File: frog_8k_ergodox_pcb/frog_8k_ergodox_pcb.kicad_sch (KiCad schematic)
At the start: 3 parts, among them J1 USB_C_Receptacle_USB2.0_14P, U1 PMW3360DM-T2QU, U2 STM32F072CBTx

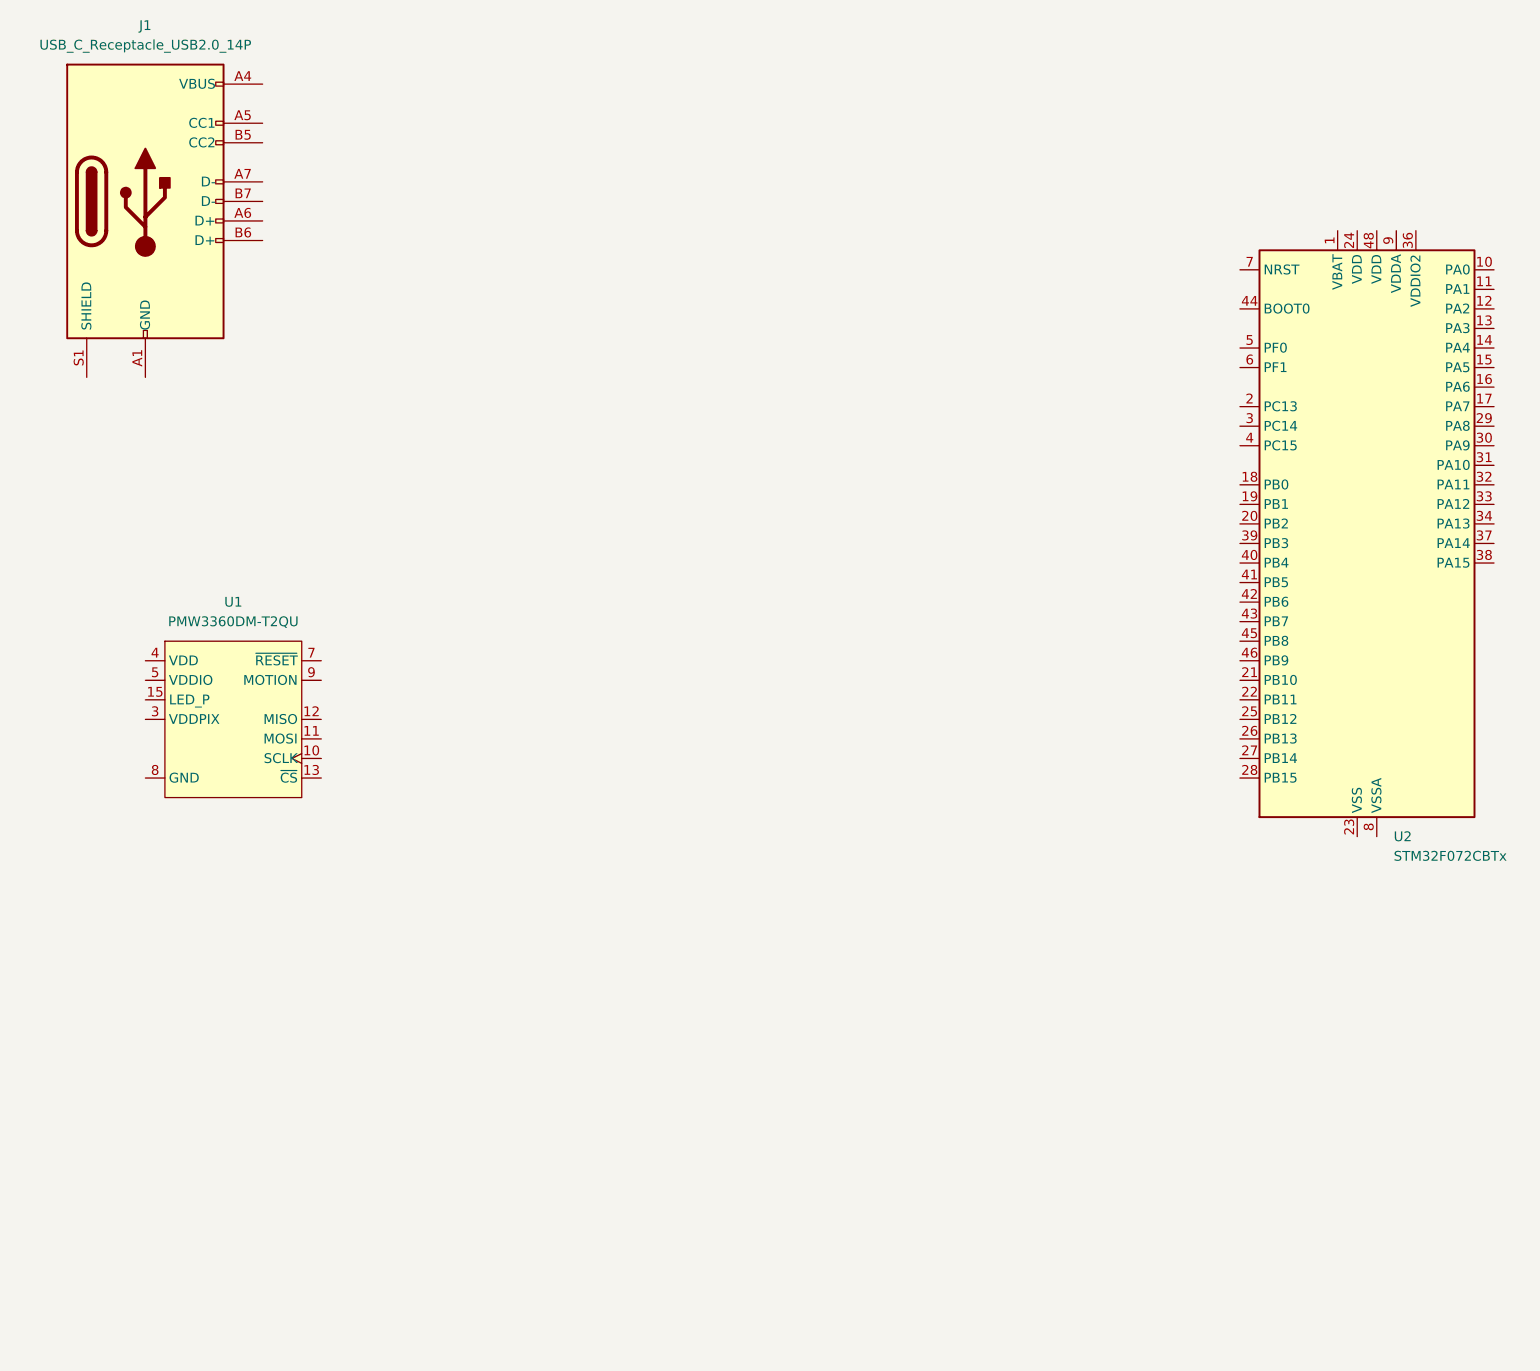
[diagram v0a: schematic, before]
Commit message: Added 3v3 power and gnd symbol
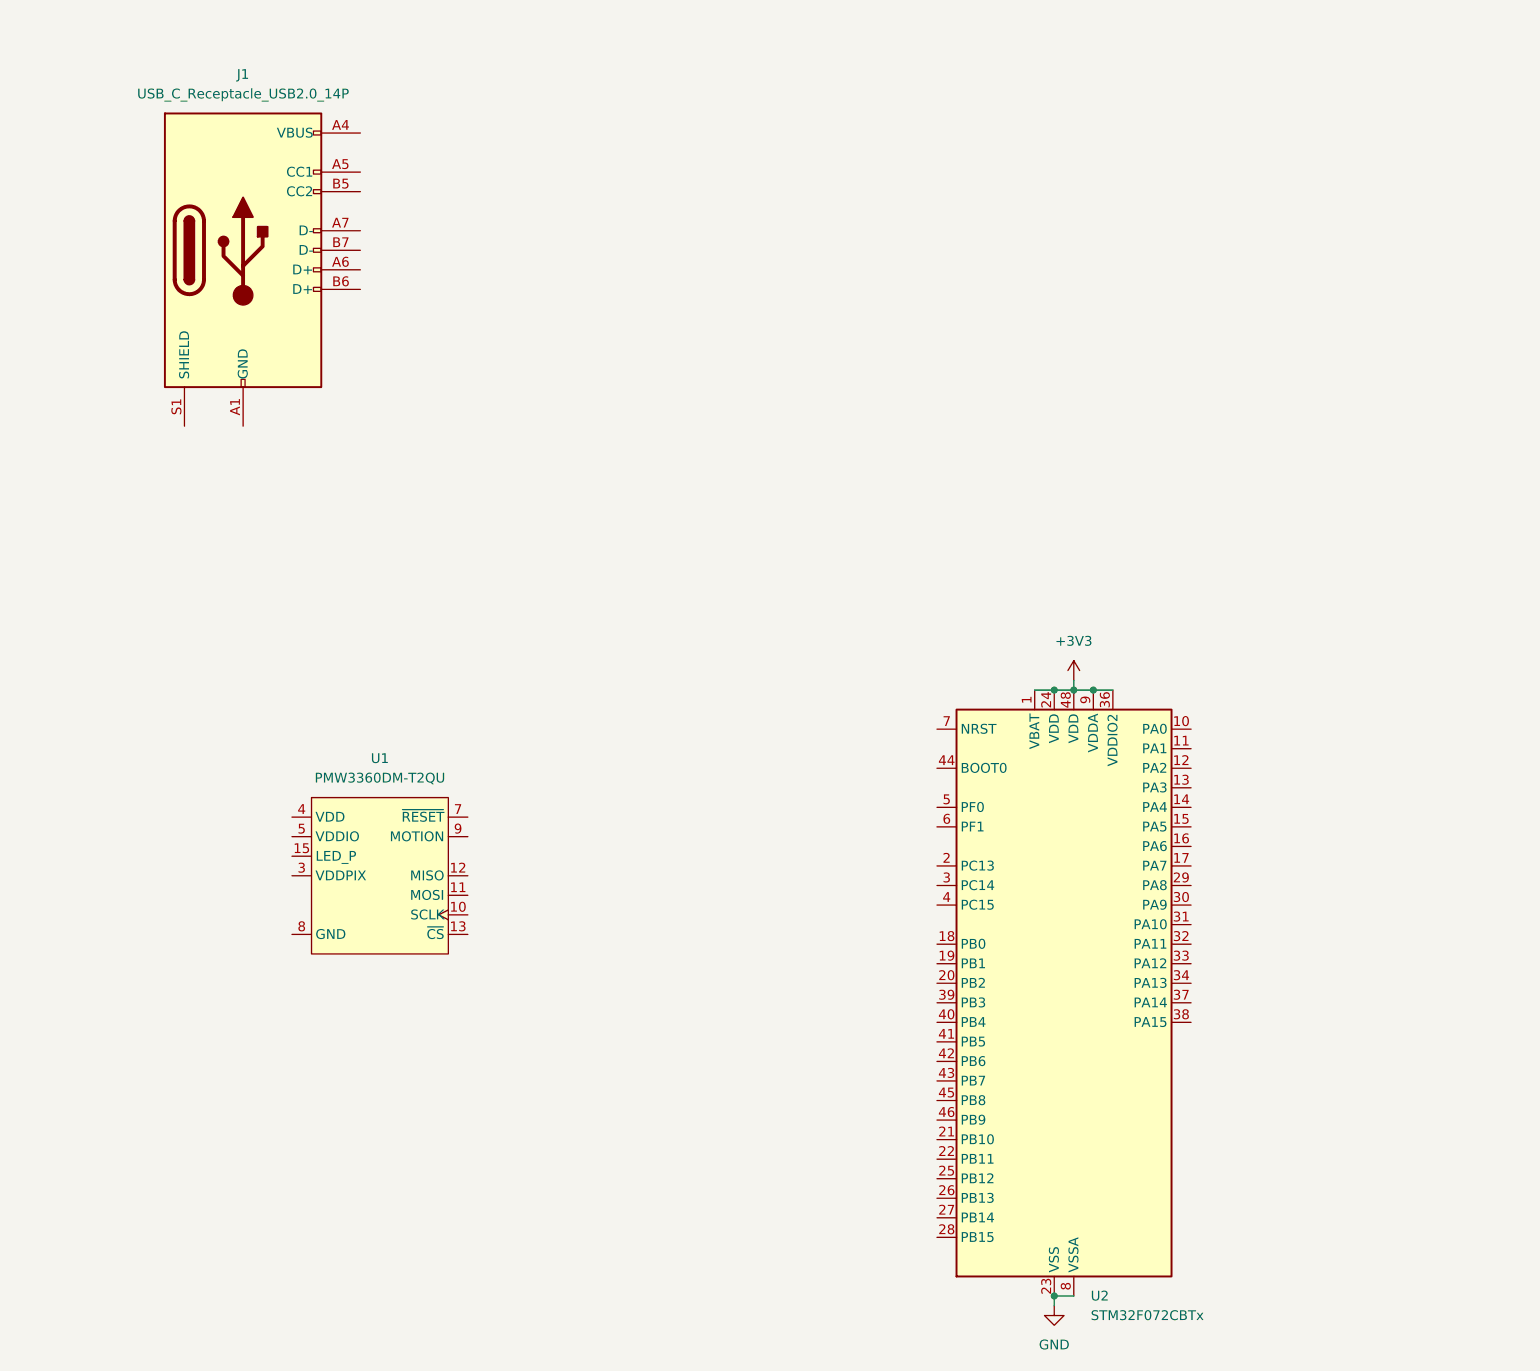
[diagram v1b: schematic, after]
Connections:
- net +3V3: now reaches U2.1 (VBAT)
- net +3V3: now also U2.24 (VDD), U2.36 (VDDIO2), U2.48 (VDD), U2.9 (VDDA)
- net GND: now reaches U2.23 (VSS), U2.35 (VSS), U2.47 (VSS)
- net GND: now also U2.8 (VSSA)
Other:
- moved on the sheet: J1, U1, U2

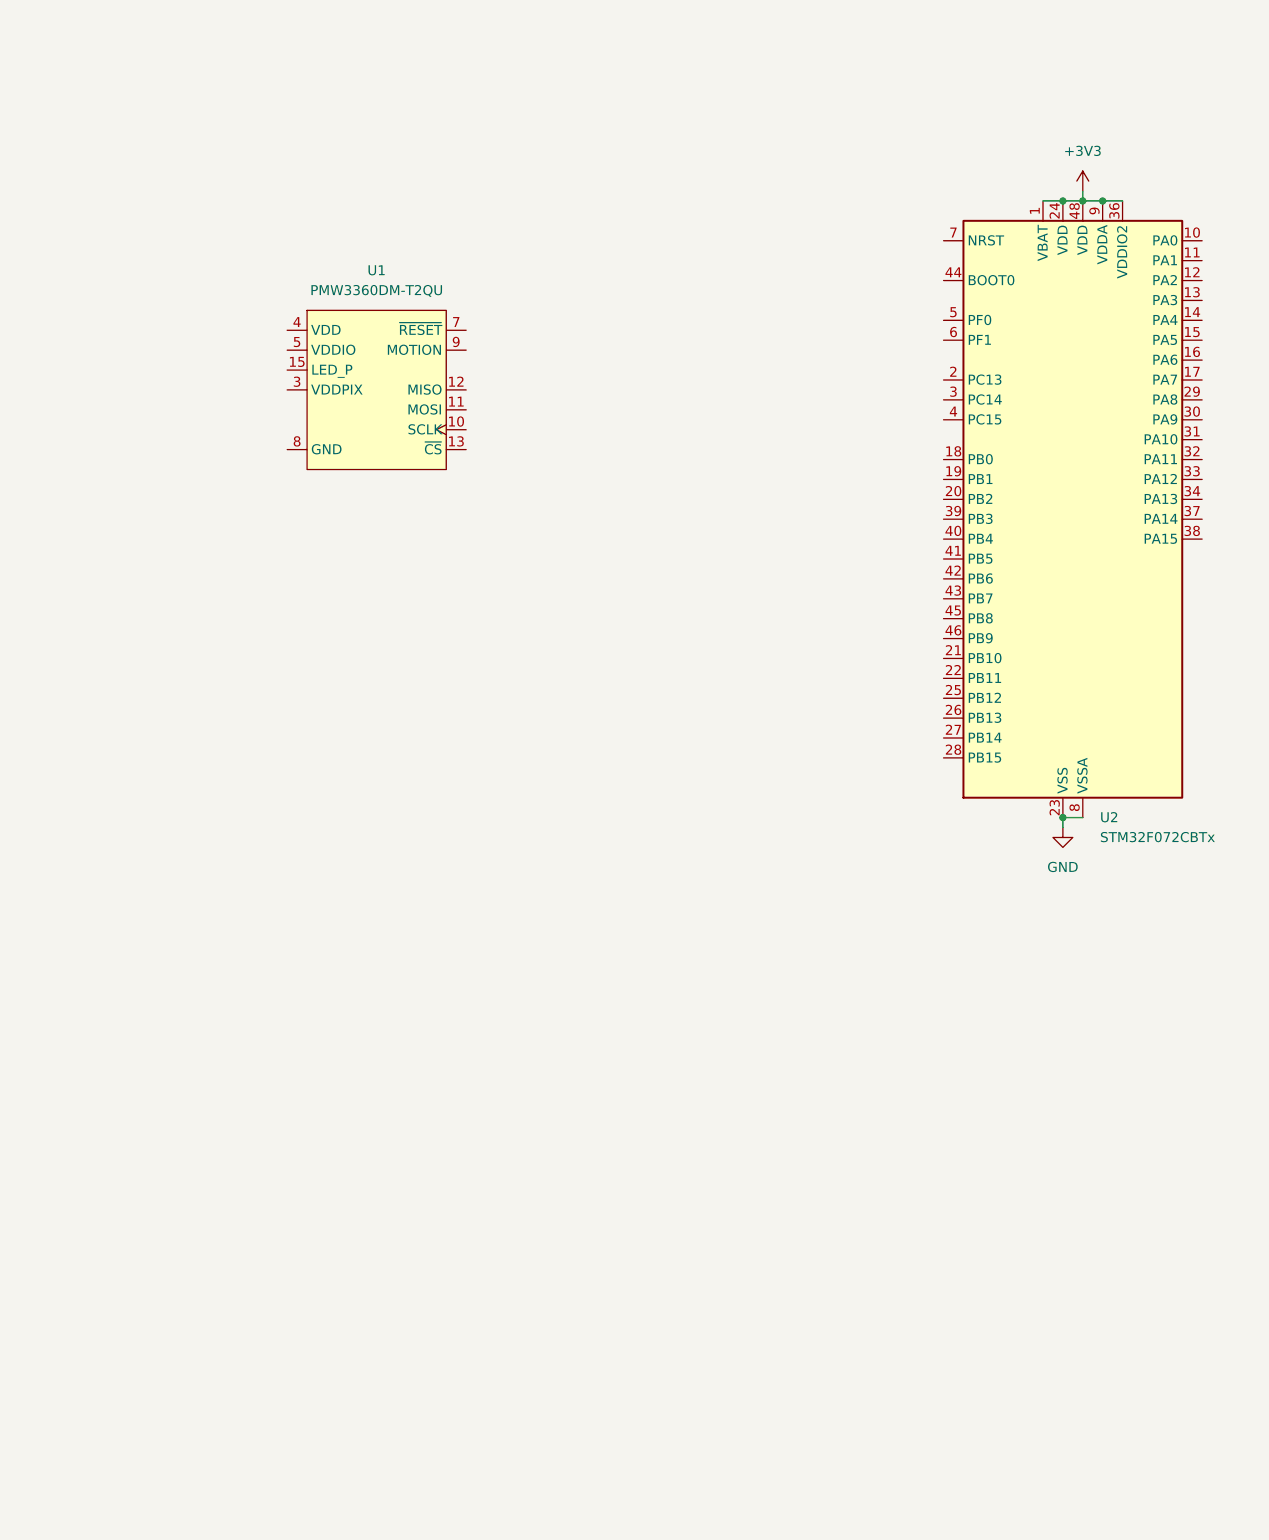
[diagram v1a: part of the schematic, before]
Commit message: Updated Capcitors and circuits for PMW3360
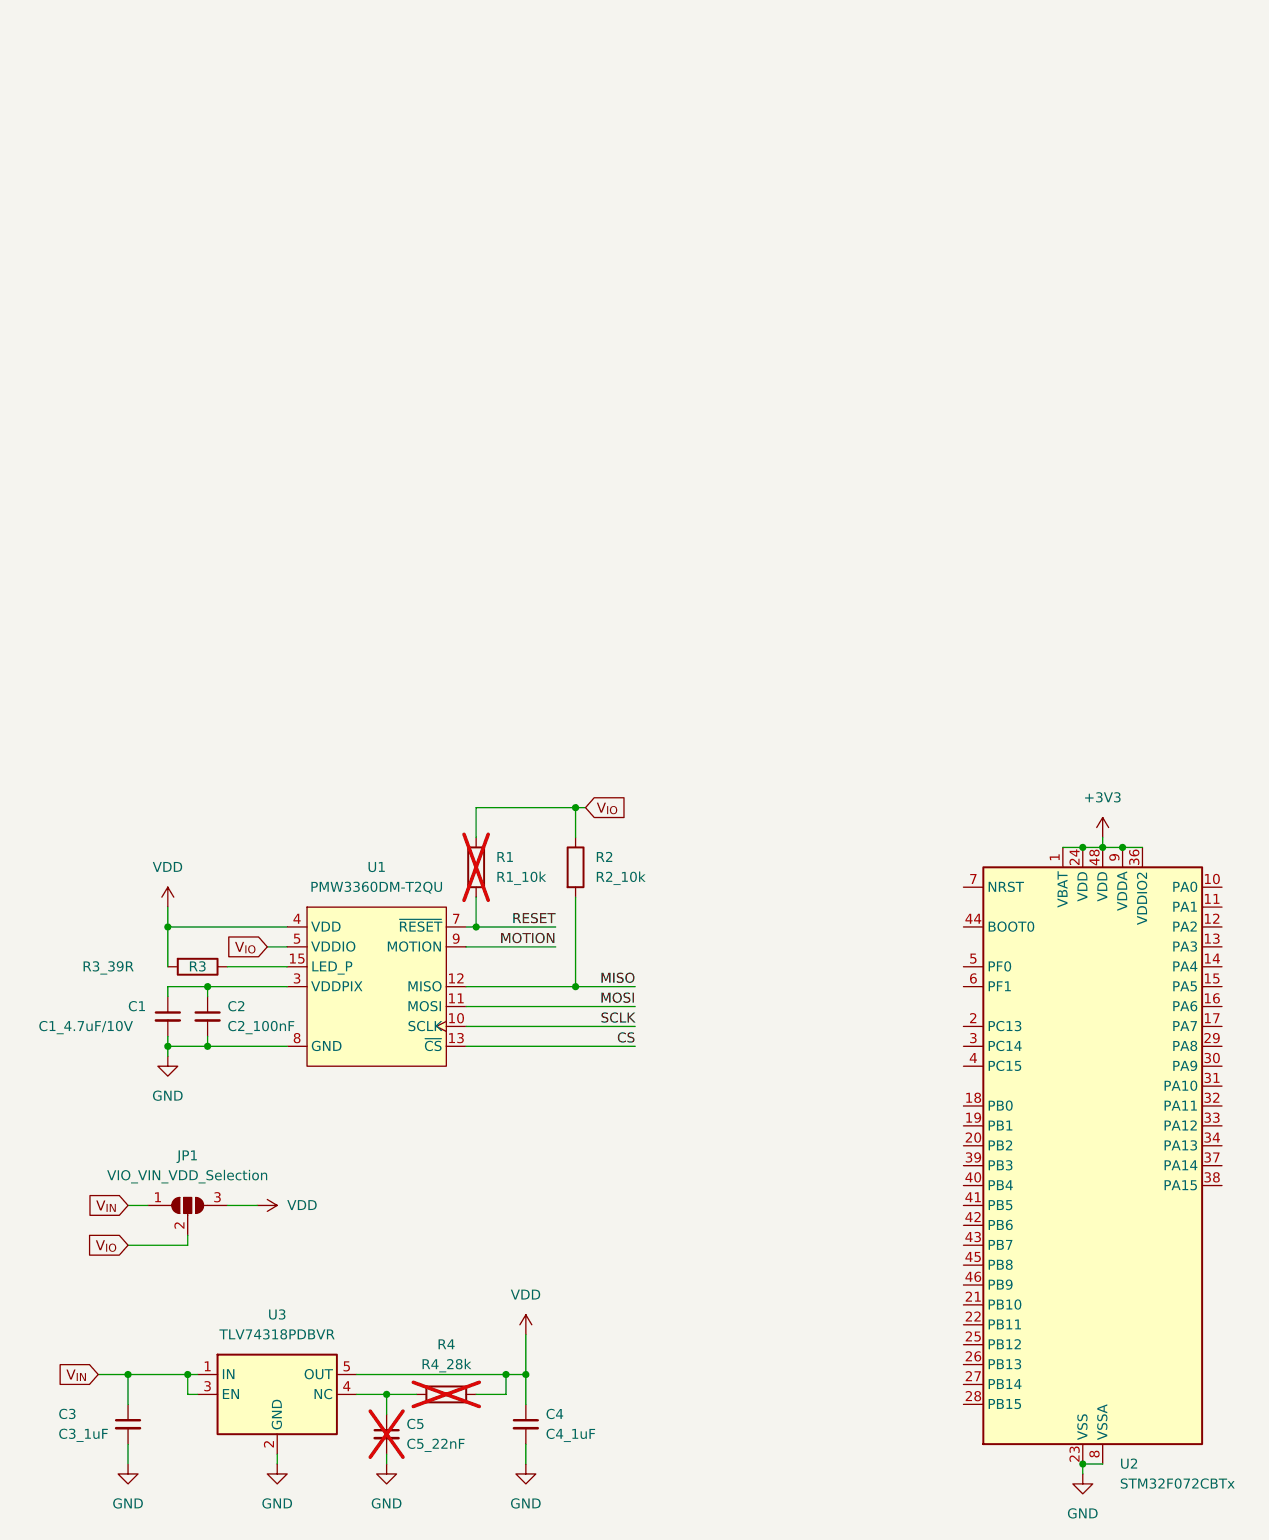
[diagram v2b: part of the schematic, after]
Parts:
- added C1: C1_4.7uF/10V, Capacitor_SMD:C_0805_2012Metric_Pad1.18x1.45mm_HandSolder, symbol Device:C_Small
- added C2: C2_100nF, Capacitor_SMD:C_0805_2012Metric_Pad1.18x1.45mm_HandSolder, symbol Device:C_Small
- added C3: C3_1uF, Capacitor_SMD:C_0805_2012Metric_Pad1.18x1.45mm_HandSolder, symbol Device:C_Small
- added C4: C4_1uF, Capacitor_SMD:C_0805_2012Metric_Pad1.18x1.45mm_HandSolder, symbol Device:C_Small
- added C5: C5_22nF, Capacitor_SMD:C_0805_2012Metric_Pad1.18x1.45mm_HandSolder, symbol Device:C_Small
- added JP1: VIO_VIN_VDD_Selection, Jumper:SolderJumper-3_P1.3mm_Open_RoundedPad1.0x1.5mm_NumberLabels, symbol Jumper:SolderJumper_3_Open
- added R1: R1_10k, Resistor_SMD:R_0805_2012Metric_Pad1.20x1.40mm_HandSolder, symbol Device:R
- added R2: R2_10k, Resistor_SMD:R_0805_2012Metric_Pad1.20x1.40mm_HandSolder, symbol Device:R
- added R3: R3_39R, Resistor_SMD:R_0805_2012Metric_Pad1.20x1.40mm_HandSolder, symbol Device:R
- added R4: R4_28k, Resistor_SMD:R_0805_2012Metric_Pad1.20x1.40mm_HandSolder, symbol Device:R
- added U3: TLV74318PDBVR, Package_TO_SOT_SMD:SOT-23-5, symbol pmw3360:TLV74318PDBVR
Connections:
- net GND: now also U1.8 (GND), C1.2, C2.2, C3.2, C4.2, C5.2, U3.2 (GND)
- net SCLK: now reaches U1.10 (SCLK)
- net MOSI: now reaches U1.11 (MOSI)
- net MISO: now reaches U1.12 (MISO)
- net MISO: now also R2.2
- net CS: now reaches U1.13 (~{CS})
- net at U1.15 (LED_P): now also R3.1
- net at U1.3 (VDDPIX): now also C1.1, C2.1
- net VDD: now reaches U1.4 (VDD)
- net VDD: now also C4.1, JP1.3 (B), R3.2, R4.1, U3.5 (OUT)
- net V_{IO}: now reaches U1.5 (VDDIO)
- net V_{IO}: now also JP1.2 (C), R1.1, R2.1
- net RESET: now reaches U1.7 (~{RESET})
- net RESET: now also R1.2
- net MOTION: now reaches U1.9 (MOTION)
- new net: C5.1, R4.2, U3.4 (NC)
- new net V_{IN}: C3.1, JP1.1 (A), U3.1 (IN), U3.3 (EN)
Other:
- title: (none) -> Frog 8K Ergodox Track Ball PCB
- moved on the sheet: U1, U2
